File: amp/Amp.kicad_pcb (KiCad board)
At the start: 2 copper layers, 128.8 x 110 mm, 45 parts, among them J1 AIN_Jack, J10 DCV_Jack, J11 EXT_IN, J12 A_OUT, J13 C_OUT, J14 B_OUT, J15 D_OUT, J16 MAIN_OUT, J17 HP_OUT, J2 BIN_Jack, J3 CIN_Jack, J4 DIN_Jack, J5 Conn_02x04_Counter_Clockwise, J6 EURORACK_CONN_16, J7 ACV_Jack, J8 BCV_Jack, J9 CCV_Jack, Q3 DMMT5401, SW1 SW_STEREO_SPLIT, U3 LM13700, U8 TL074

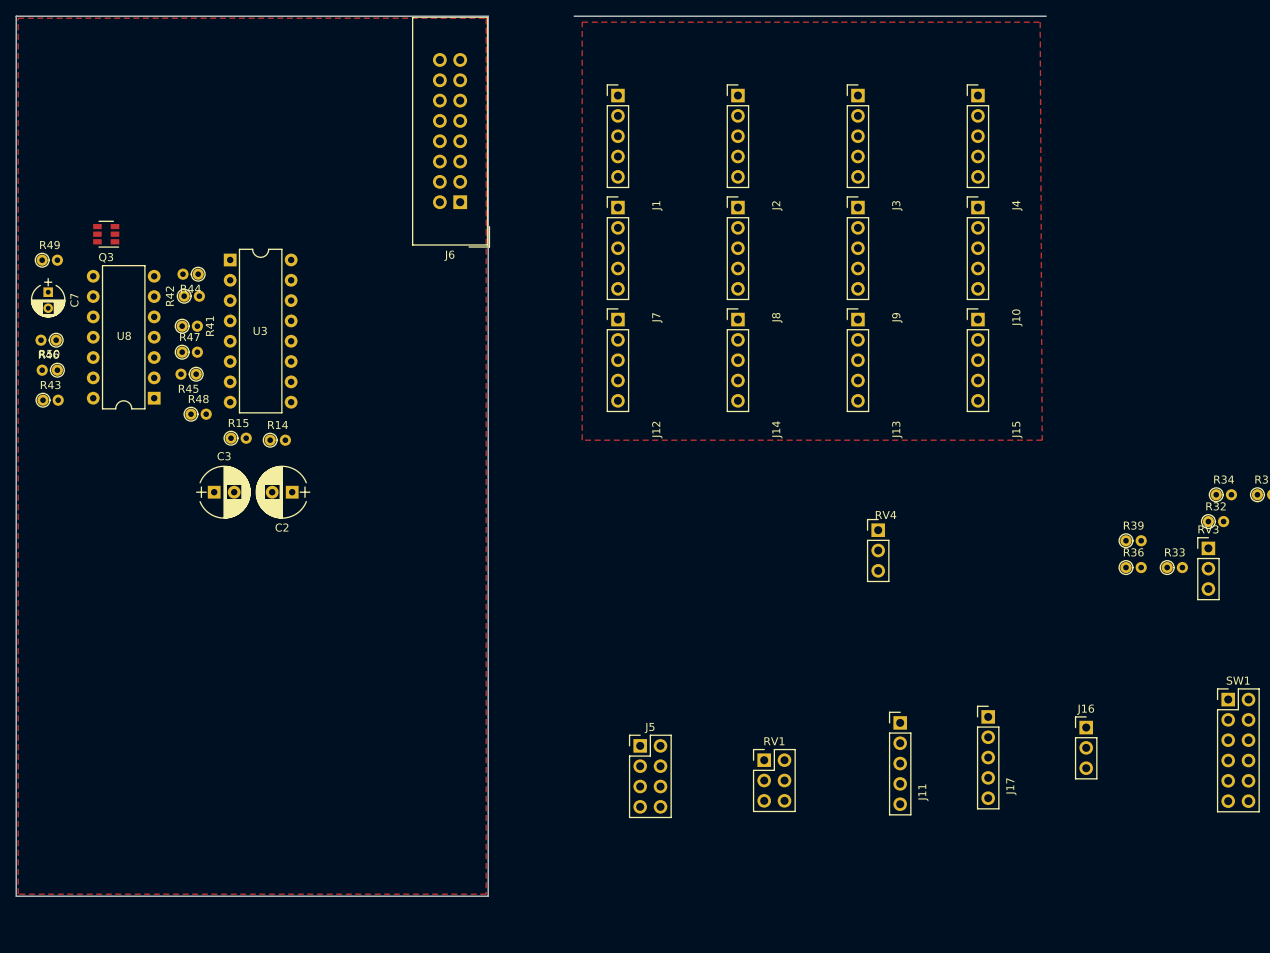
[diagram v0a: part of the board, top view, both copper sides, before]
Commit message: more vca layout
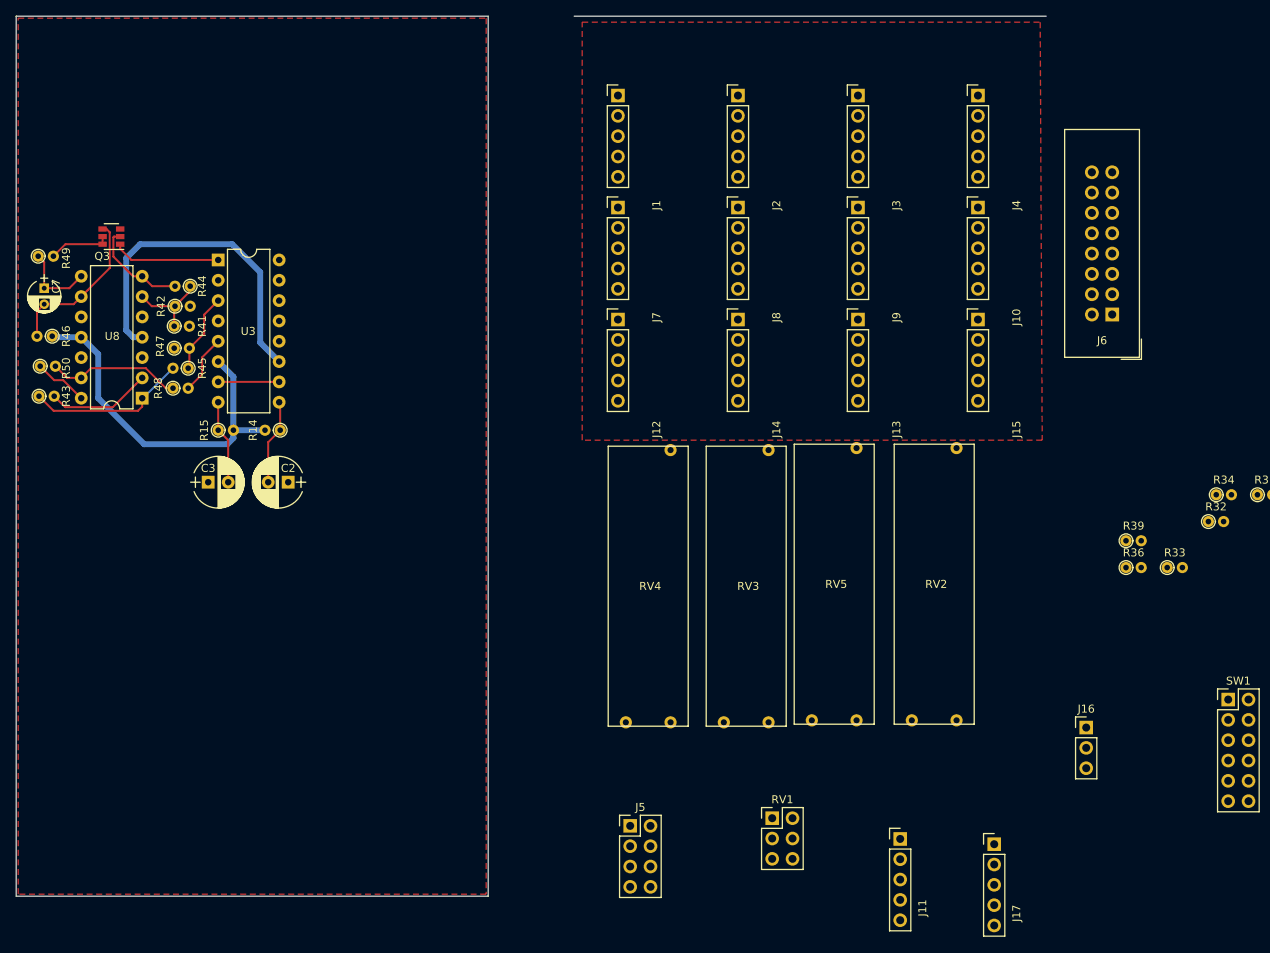
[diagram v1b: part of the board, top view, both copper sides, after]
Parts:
- added RV2: 10K, synth:slide_potentiometer_35mm, F.Cu at (200.5, 101.5)
- added RV5: 10K, synth:slide_potentiometer_35mm, F.Cu at (188.0, 101.5)
- RV3, RV4: value 100K -> 10K; footprint KiCad/kicad-footprints/Connector_PinHeader_2.54mm.pretty:PinHeader_1x03_P2.54mm_Vertical -> synth:slide_potentiometer_35mm
- moved J6 82.7 mm to (222.8, 67.8)
- moved RV3 58.0 mm to (177.0, 101.8)
- moved RV4 29.6 mm to (164.8, 101.8)
- moved J17 15.9 mm to (208.0, 134.0)
- moved J11 14.5 mm to (196.2, 133.3)
- moved J5 10.1 mm to (162.5, 131.7)
- moved RV1 7.32 mm to (180.2, 130.8)
- moved R48 3.95 mm to (105.3, 77.0)
- moved R50 2.21 mm to (88.8, 74.2), turned to 0 degrees
- moved R15 1.89 mm to (111.0, 82.2)
- moved R44 1.80 mm to (107.5, 64.2)
- moved R14 1.77 mm to (118.8, 82.2), turned to 180 degrees
- moved R42 1.70 mm to (105.6, 66.8)
- moved U3 1.50 mm to (111.0, 61.0)
- moved U8 1.50 mm to (101.5, 78.2)
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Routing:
- net -12VA: track 0.00 -> 46.1 mm
- net +12VA: track 0.00 -> 42.4 mm
- net Net-(R43-Pad1): track 0.00 -> 20.3 mm
- net Net-(C7-Pad2): track 0.00 -> 20.0 mm
- net Net-(R48-Pad1): track 0.00 -> 16.8 mm
- net Net-(Q3-Pad1): track 0.00 -> 13.4 mm
- net D_IN: track 0.00 -> 13.1 mm
- net Net-(Q3-Pad2): track 0.00 -> 12.5 mm
- net Net-(C2-Pad2): track 0.00 -> 10.7 mm
- net Net-(C3-Pad2): track 0.00 -> 10.5 mm
- net Net-(R41-Pad1): track 0.00 -> 10.4 mm
- net Net-(R45-Pad1): track 0.00 -> 10.0 mm
- net Net-(C7-Pad1): track 0.00 -> 9.56 mm
- net Net-(Q3-Pad5): track 0.00 -> 7.72 mm
- net Net-(RV1-Pad5): track 0.00 -> 7.62 mm
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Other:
- board text added: "TODO: measure from origin outside of board"

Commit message: update amp
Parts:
- added C6: 30p, KiCad/Capacitors_ThroughHole.pretty:CP_Radial_D4.0mm_P2.00mm, F.Cu at (133.1, 40.4)
- added Q2: DMMT5401, KiCad/kicad-footprints/Package_TO_SOT_SMD.pretty:SOT-23-6, F.Cu at (126.0, 53.8)
- added R35: 820K, KiCad/Resistors_ThroughHole.pretty:R_Axial_DIN0204_L3.6mm_D1.6mm_P1.90mm_Vertical, F.Cu at (132.6, 48.3)
- added R38: 13K, KiCad/Resistors_ThroughHole.pretty:R_Axial_DIN0204_L3.6mm_D1.6mm_P1.90mm_Vertical, F.Cu at (132.6, 44.9)
- added U7: TL074, KiCad/Housings_DIP.pretty:DIP-14_W7.62mm, F.Cu at (136.8, 78.8)
- moved R31 125.6 mm to (126.2, 39.3)
- moved R32 125.6 mm to (120.0, 42.7)
- moved R33 125.6 mm to (114.9, 48.4)
- moved R34 125.6 mm to (121.0, 39.3)
- moved R36 125.6 mm to (109.7, 48.4)
- moved R39 125.6 mm to (109.7, 45.1)

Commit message: update components
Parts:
- removed the R35 at (132.6, 48.3)
- removed the R41 at (105.5, 69.2)
- removed the R45 at (107.2, 74.5)
- removed the R47 at (105.5, 72.0)
- added C1: 2.2u, Capacitor_THT:C_Radial_D6.3mm_H5.0mm_P2.50mm, F.Cu at (165.8, 168.2)
- added C4: 2.2u, Capacitor_THT:C_Radial_D6.3mm_H5.0mm_P2.50mm, F.Cu at (173.5, 166.0)
- added C5: 30p, Capacitor_THT:C_Disc_D3.0mm_W2.0mm_P2.50mm, F.Cu at (254.7, 83.0)
- added C8: 30p, Capacitor_THT:C_Disc_D3.0mm_W2.0mm_P2.50mm, F.Cu at (254.7, 97.8)
- added Q1: DMMT5401, Package_TO_SOT_SMD:SOT-23-6, F.Cu at (288.8, 36.8)
- added Q4: DMMT5401, Package_TO_SOT_SMD:SOT-23-6, F.Cu at (288.8, 60.0)
- added R1: 200K, Resistor_THT:R_Axial_DIN0204_L3.6mm_D1.6mm_P1.90mm_Vertical, F.Cu at (239.9, 95.5)
- added R10: 200K, Resistor_THT:R_Axial_DIN0204_L3.6mm_D1.6mm_P1.90mm_Vertical, F.Cu at (230.0, 89.2)
- added R11: 200K, Resistor_THT:R_Axial_DIN0204_L3.6mm_D1.6mm_P1.90mm_Vertical, F.Cu at (235.0, 86.0)
- added R12: 200K, Resistor_THT:R_Axial_DIN0204_L3.6mm_D1.6mm_P1.90mm_Vertical, F.Cu at (239.9, 82.9)
- added R13: 10K, Resistor_THT:R_Axial_DIN0204_L3.6mm_D1.6mm_P1.90mm_Vertical, F.Cu at (166.8, 176.2)
- added R16: 10K, Resistor_THT:R_Axial_DIN0204_L3.6mm_D1.6mm_P1.90mm_Vertical, F.Cu at (174.2, 184.0)
- added R17: 470, Resistor_THT:R_Axial_DIN0204_L3.6mm_D1.6mm_P1.90mm_Vertical, F.Cu at (180.4, 160.3)
- added R18: 470, Resistor_THT:R_Axial_DIN0204_L3.6mm_D1.6mm_P1.90mm_Vertical, F.Cu at (180.0, 171.2)
- added R19: 470, Resistor_THT:R_Axial_DIN0204_L3.6mm_D1.6mm_P1.90mm_Vertical, F.Cu at (185.4, 157.2)
- added R2: 200K, Resistor_THT:R_Axial_DIN0204_L3.6mm_D1.6mm_P1.90mm_Vertical, F.Cu at (244.9, 89.2)
- added R20: 470, Resistor_THT:R_Axial_DIN0204_L3.6mm_D1.6mm_P1.90mm_Vertical, F.Cu at (185.0, 168.1)
- added R21: 820K, Resistor_THT:R_Axial_DIN0204_L3.6mm_D1.6mm_P1.90mm_Vertical, F.Cu at (269.5, 86.0)
- added R22: 120K, Resistor_THT:R_Axial_DIN0204_L3.6mm_D1.6mm_P1.90mm_Vertical, F.Cu at (264.6, 89.2)
- added R23: 270K, Resistor_THT:R_Axial_DIN0204_L3.6mm_D1.6mm_P1.90mm_Vertical, F.Cu at (264.6, 86.0)
- added R24: 3K3, Resistor_THT:R_Axial_DIN0204_L3.6mm_D1.6mm_P1.90mm_Vertical, F.Cu at (259.6, 89.5)
- added R25: 3K3, Resistor_THT:R_Axial_DIN0204_L3.6mm_D1.6mm_P1.90mm_Vertical, F.Cu at (267.8, 82.9)
- added R26: 22K, Resistor_THT:R_Axial_DIN0204_L3.6mm_D1.6mm_P1.90mm_Vertical, F.Cu at (259.6, 86.3)
- added R27: 27K, Resistor_THT:R_Axial_DIN0204_L3.6mm_D1.6mm_P1.90mm_Vertical, F.Cu at (254.7, 89.5)
- added R28: 5K, Resistor_THT:R_Axial_DIN0204_L3.6mm_D1.6mm_P1.90mm_Vertical, F.Cu at (262.8, 82.9)
- added R29: 22K, Resistor_THT:R_Axial_DIN0204_L3.6mm_D1.6mm_P1.90mm_Vertical, F.Cu at (254.7, 86.3)
- added R3: 200K, Resistor_THT:R_Axial_DIN0204_L3.6mm_D1.6mm_P1.90mm_Vertical, F.Cu at (239.9, 92.3)
- added R30: 820K, Resistor_THT:R_Axial_DIN0204_L3.6mm_D1.6mm_P1.90mm_Vertical, F.Cu at (222.2, 102.5)
- added R38: 22K, Resistor_THT:R_Axial_DIN0204_L3.6mm_D1.6mm_P1.90mm_Vertical, F.Cu at (227.1, 102.5)
- added R39: 820K, Resistor_THT:R_Axial_DIN0204_L3.6mm_D1.6mm_P1.90mm_Vertical, F.Cu at (235.1, 102.5)
- added R4: 200K, Resistor_THT:R_Axial_DIN0204_L3.6mm_D1.6mm_P1.90mm_Vertical, F.Cu at (235.0, 95.5)
- added R40: 120K, Resistor_THT:R_Axial_DIN0204_L3.6mm_D1.6mm_P1.90mm_Vertical, F.Cu at (105.1, 76.8)
- added R48: 820K, Resistor_THT:R_Axial_DIN0204_L3.6mm_D1.6mm_P1.90mm_Vertical, F.Cu at (254.7, 101.2)
- added R49: 120K, Resistor_THT:R_Axial_DIN0204_L3.6mm_D1.6mm_P1.90mm_Vertical, F.Cu at (262.8, 97.7)
- added R5: 200K, Resistor_THT:R_Axial_DIN0204_L3.6mm_D1.6mm_P1.90mm_Vertical, F.Cu at (244.9, 86.0)
- added R50: 270K, Resistor_THT:R_Axial_DIN0204_L3.6mm_D1.6mm_P1.90mm_Vertical, F.Cu at (254.7, 104.3)
- added R51: 3K3, Resistor_THT:R_Axial_DIN0204_L3.6mm_D1.6mm_P1.90mm_Vertical, F.Cu at (259.6, 101.2)
- added R52: 3K3, Resistor_THT:R_Axial_DIN0204_L3.6mm_D1.6mm_P1.90mm_Vertical, F.Cu at (267.8, 97.7)
- added R53: 22K, Resistor_THT:R_Axial_DIN0204_L3.6mm_D1.6mm_P1.90mm_Vertical, F.Cu at (259.6, 104.3)
- added R54: 27K, Resistor_THT:R_Axial_DIN0204_L3.6mm_D1.6mm_P1.90mm_Vertical, F.Cu at (264.6, 100.8)
- added R55: 5K, Resistor_THT:R_Axial_DIN0204_L3.6mm_D1.6mm_P1.90mm_Vertical, F.Cu at (264.6, 104.0)
- added R56: 22K, Resistor_THT:R_Axial_DIN0204_L3.6mm_D1.6mm_P1.90mm_Vertical, F.Cu at (269.5, 100.8)
- added R6: 200K, Resistor_THT:R_Axial_DIN0204_L3.6mm_D1.6mm_P1.90mm_Vertical, F.Cu at (239.9, 89.2)
- added R7: 200K, Resistor_THT:R_Axial_DIN0204_L3.6mm_D1.6mm_P1.90mm_Vertical, F.Cu at (230.0, 82.9)
- added R8: 200K, Resistor_THT:R_Axial_DIN0204_L3.6mm_D1.6mm_P1.90mm_Vertical, F.Cu at (235.0, 82.9)
- added R9: 200K, Resistor_THT:R_Axial_DIN0204_L3.6mm_D1.6mm_P1.90mm_Vertical, F.Cu at (230.0, 86.0)
- added RT1: 50K, Resistor_THT:R_Box_L14.0mm_W5.0mm_P9.00mm, F.Cu at (314.8, 77.0)
- added RT10: 50K, Resistor_THT:R_Box_L14.0mm_W5.0mm_P9.00mm, F.Cu at (379.8, 144.0)
- added RT11: 5K, Resistor_THT:R_Box_L14.0mm_W5.0mm_P9.00mm, F.Cu at (386.0, 134.0)
- added RT12: 10K, Resistor_THT:R_Box_L14.0mm_W5.0mm_P9.00mm, F.Cu at (330.3, 99.2)
- added RT2: 5K, Resistor_THT:R_Box_L14.0mm_W5.0mm_P9.00mm, F.Cu at (314.8, 83.5)
- added RT3: 10K, Resistor_THT:R_Box_L14.0mm_W5.0mm_P9.00mm, F.Cu at (337.5, 53.5)
- added RT4: 50K, Resistor_THT:R_Box_L14.0mm_W5.0mm_P9.00mm, F.Cu at (117.5, 22.0)
- added RT5: 5K, Resistor_THT:R_Box_L14.0mm_W5.0mm_P9.00mm, F.Cu at (102.8, 22.0)
- added RT6: 10K, Resistor_THT:R_Box_L14.0mm_W5.0mm_P9.00mm, F.Cu at (148.5, 69.2)
- added RT7: 50K, Resistor_THT:R_Box_L14.0mm_W5.0mm_P9.00mm, F.Cu at (106.2, 66.8)
- added RT8: 5K, Resistor_THT:R_Box_L14.0mm_W5.0mm_P9.00mm, F.Cu at (89.0, 56.8)
- added RT9: 10K, Resistor_THT:R_Box_L14.0mm_W5.0mm_P9.00mm, F.Cu at (89.0, 80.5)
- added U1: TL074, Package_DIP:DIP-14_W7.62mm, F.Cu at (243.6, 36.5)
- added U2: LM13700, Package_DIP:DIP-16_W7.62mm, F.Cu at (232.8, 36.5)
- added U4: TL072, Package_DIP:DIP-8_W7.62mm, F.Cu at (232.8, 62.8)
- added U5: TL074, Package_DIP:DIP-14_W7.62mm, F.Cu at (277.1, 36.5)
- added U8: TL074, Package_DIP:DIP-14_W7.62mm, F.Cu at (277.1, 59.8)
- C2, C3: footprint KiCad/Capacitors_ThroughHole.pretty:CP_Radial_D6.3mm_P2.50mm -> Capacitor_THT:C_Radial_D6.3mm_H5.0mm_P2.50mm
- C6, C7: footprint KiCad/Capacitors_ThroughHole.pretty:CP_Radial_D4.0mm_P2.00mm -> Capacitor_THT:C_Disc_D3.0mm_W2.0mm_P2.50mm
- J16: footprint KiCad/kicad-footprints/Connector_PinHeader_2.54mm.pretty:PinHeader_1x03_P2.54mm_Vertical -> Connector_PinHeader_2.54mm:PinHeader_1x03_P2.54mm_Vertical
- J5: footprint KiCad/kicad-footprints/Connector_PinHeader_2.54mm.pretty:PinHeader_2x04_P2.54mm_Vertical -> Connector_PinHeader_2.54mm:PinHeader_2x04_P2.54mm_Vertical
- Q2, Q3: footprint KiCad/kicad-footprints/Package_TO_SOT_SMD.pretty:SOT-23-6 -> Package_TO_SOT_SMD:SOT-23-6
- R14, R15: footprint KiCad/Resistors_ThroughHole.pretty:R_Axial_DIN0204_L3.6mm_D1.6mm_P1.90mm_Vertical -> Resistor_THT:R_Axial_DIN0204_L3.6mm_D1.6mm_P1.90mm_Vertical
- R31: value 100K -> 120K; footprint KiCad/Resistors_ThroughHole.pretty:R_Axial_DIN0204_L3.6mm_D1.6mm_P1.90mm_Vertical -> Resistor_THT:R_Axial_DIN0204_L3.6mm_D1.6mm_P1.90mm_Vertical
- R32: value 220K -> 270K; footprint KiCad/Resistors_ThroughHole.pretty:R_Axial_DIN0204_L3.6mm_D1.6mm_P1.90mm_Vertical -> Resistor_THT:R_Axial_DIN0204_L3.6mm_D1.6mm_P1.90mm_Vertical
- R33: value 10K -> 3K3; footprint KiCad/Resistors_ThroughHole.pretty:R_Axial_DIN0204_L3.6mm_D1.6mm_P1.90mm_Vertical -> Resistor_THT:R_Axial_DIN0204_L3.6mm_D1.6mm_P1.90mm_Vertical
- R34: value 1K8 -> 3K3; footprint KiCad/Resistors_ThroughHole.pretty:R_Axial_DIN0204_L3.6mm_D1.6mm_P1.90mm_Vertical -> Resistor_THT:R_Axial_DIN0204_L3.6mm_D1.6mm_P1.90mm_Vertical
- R35: renamed from R36; value 12K -> 22K; footprint KiCad/Resistors_ThroughHole.pretty:R_Axial_DIN0204_L3.6mm_D1.6mm_P1.90mm_Vertical -> Resistor_THT:R_Axial_DIN0204_L3.6mm_D1.6mm_P1.90mm_Vertical
- R36: renamed from R38; value 13K -> 27K; footprint KiCad/Resistors_ThroughHole.pretty:R_Axial_DIN0204_L3.6mm_D1.6mm_P1.90mm_Vertical -> Resistor_THT:R_Axial_DIN0204_L3.6mm_D1.6mm_P1.90mm_Vertical
- R37: renamed from R39; footprint KiCad/Resistors_ThroughHole.pretty:R_Axial_DIN0204_L3.6mm_D1.6mm_P1.90mm_Vertical -> Resistor_THT:R_Axial_DIN0204_L3.6mm_D1.6mm_P1.90mm_Vertical
- R41: renamed from R42; value 220K -> 270K; footprint KiCad/Resistors_ThroughHole.pretty:R_Axial_DIN0204_L3.6mm_D1.6mm_P1.90mm_Vertical -> Resistor_THT:R_Axial_DIN0204_L3.6mm_D1.6mm_P1.90mm_Vertical
- R42: renamed from R43; value 10K -> 3K3; footprint KiCad/Resistors_ThroughHole.pretty:R_Axial_DIN0204_L3.6mm_D1.6mm_P1.90mm_Vertical -> Resistor_THT:R_Axial_DIN0204_L3.6mm_D1.6mm_P1.90mm_Vertical
- R43: renamed from R44; value 1K8 -> 3K3; footprint KiCad/Resistors_ThroughHole.pretty:R_Axial_DIN0204_L3.6mm_D1.6mm_P1.90mm_Vertical -> Resistor_THT:R_Axial_DIN0204_L3.6mm_D1.6mm_P1.90mm_Vertical
- R44: renamed from R46; value 12K -> 22K; footprint KiCad/Resistors_ThroughHole.pretty:R_Axial_DIN0204_L3.6mm_D1.6mm_P1.90mm_Vertical -> Resistor_THT:R_Axial_DIN0204_L3.6mm_D1.6mm_P1.90mm_Vertical
- R45: renamed from R48; value 13K -> 27K; footprint KiCad/Resistors_ThroughHole.pretty:R_Axial_DIN0204_L3.6mm_D1.6mm_P1.90mm_Vertical -> Resistor_THT:R_Axial_DIN0204_L3.6mm_D1.6mm_P1.90mm_Vertical
- R46: renamed from R49; footprint KiCad/Resistors_ThroughHole.pretty:R_Axial_DIN0204_L3.6mm_D1.6mm_P1.90mm_Vertical -> Resistor_THT:R_Axial_DIN0204_L3.6mm_D1.6mm_P1.90mm_Vertical
- R47: renamed from R50; value 13K -> 22K; footprint KiCad/Resistors_ThroughHole.pretty:R_Axial_DIN0204_L3.6mm_D1.6mm_P1.90mm_Vertical -> Resistor_THT:R_Axial_DIN0204_L3.6mm_D1.6mm_P1.90mm_Vertical
- RV1: footprint KiCad/kicad-footprints/Connector_PinHeader_2.54mm.pretty:PinHeader_2x03_P2.54mm_Vertical -> Connector_PinHeader_2.54mm:PinHeader_2x03_P2.54mm_Vertical
- SW1: footprint KiCad/kicad-footprints/Connector_PinHeader_2.54mm.pretty:PinHeader_2x06_P2.54mm_Vertical -> Connector_PinHeader_2.54mm:PinHeader_2x06_P2.54mm_Vertical
- U3: footprint KiCad/Housings_DIP.pretty:DIP-16_W7.62mm -> Package_DIP:DIP-16_W7.62mm
- U6: renamed from U7; footprint KiCad/Housings_DIP.pretty:DIP-14_W7.62mm -> Package_DIP:DIP-14_W7.62mm
- U7: renamed from U8; footprint KiCad/Housings_DIP.pretty:DIP-14_W7.62mm -> Package_DIP:DIP-14_W7.62mm
- moved C2 88.7 mm to (175.8, 157.5)
- moved C3 88.7 mm to (165.8, 157.5)
- moved R14 88.7 mm to (174.8, 151.0)
- moved R15 88.7 mm to (167.0, 151.0)
- moved J16 46.0 mm to (198.2, 160.2)
- moved SW1 23.6 mm to (225.8, 136.5)
- moved R44 16.5 mm to (95.0, 54.8), turned to 0 degrees
- moved R42 12.0 mm to (100.0, 81.8), turned to 180 degrees
- moved R47 8.88 mm to (93.5, 81.8)
- moved R46 8.27 mm to (96.8, 60.0), turned to 90 degrees
- moved Q2 7.62 mm to (131.8, 58.8)
- moved R41 7.52 mm to (105.1, 74.2)
- moved R43 7.52 mm to (107.0, 71.8)
- moved C7 6.72 mm to (94.0, 59.8), turned to 90 degrees
- moved C6 5.40 mm to (131.9, 35.1)
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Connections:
- R33 pad 2: C_IN -> Net-(R30-Pad1)
- R35 pad 1: -12VA -> Net-(R35-Pad1)
- R41 pad 2: Net-(R42-Pad2) -> Net-(R41-Pad2)
- R42 pad 1: Net-(R43-Pad1) -> Net-(R42-Pad1)
- R42 pad 2: D_IN -> Net-(R39-Pad1)
- R44 pad 1: -12VA -> Net-(R44-Pad1)
- R47 pad 1: D_OUT -> Net-(R47-Pad1)
- RV3 pad 2: Net-(R32-Pad2) -> Net-(RT4-Pad2)
- RV4 pad 2: Net-(R42-Pad2) -> Net-(RT7-Pad2)
- U3 pad 14: Net-(R35-Pad1) -> Net-(R33-Pad1)
- U3 pad 3: Net-(R45-Pad1) (its old number) -> Net-(R42-Pad1)
- U6 pad 2: C_IN -> Net-(R30-Pad1)
- U7 pad 1: Net-(R43-Pad1) -> Net-(R42-Pad1)
- U7 pad 2: D_IN -> Net-(R39-Pad1)
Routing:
- net +12VA: track 42.4 -> 0.00 mm
- net -12VA: track 46.1 -> 9.59 mm
- net Net-(R43-Pad1): track 20.3 -> 0.00 mm
- net D_IN: track 13.1 -> 0.00 mm
- net Net-(C3-Pad2): track 10.5 -> 0.00 mm
- net Net-(C2-Pad2): track 10.7 -> 0.18 mm
- net Net-(R45-Pad1) (its old number): track 10.0 -> 0.00 mm
- net Net-(R41-Pad2): track 0.00 -> 8.66 mm
- net Net-(R45-Pad2): track 7.42 -> 16.0 mm
- net Net-(RV1-Pad5): track 7.62 -> 0.00 mm
- net Net-(R39-Pad1): track 0.00 -> 7.45 mm
- net Net-(R44-Pad1): track 0.00 -> 6.83 mm
- net Net-(R40-Pad1): track 10.4 -> 16.0 mm
- net Net-(R47-Pad1): track 0.00 -> 5.02 mm
- net Net-(Q3-Pad5): track 7.72 -> 3.16 mm
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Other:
- board text added: "29mm x 29mm"
